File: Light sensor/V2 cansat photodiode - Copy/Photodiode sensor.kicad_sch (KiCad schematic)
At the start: 23 parts, among them IC1 MCP6004-I_SL, J1 Conn_01x02, J2 Conn_01x05, J3 Conn_01x04

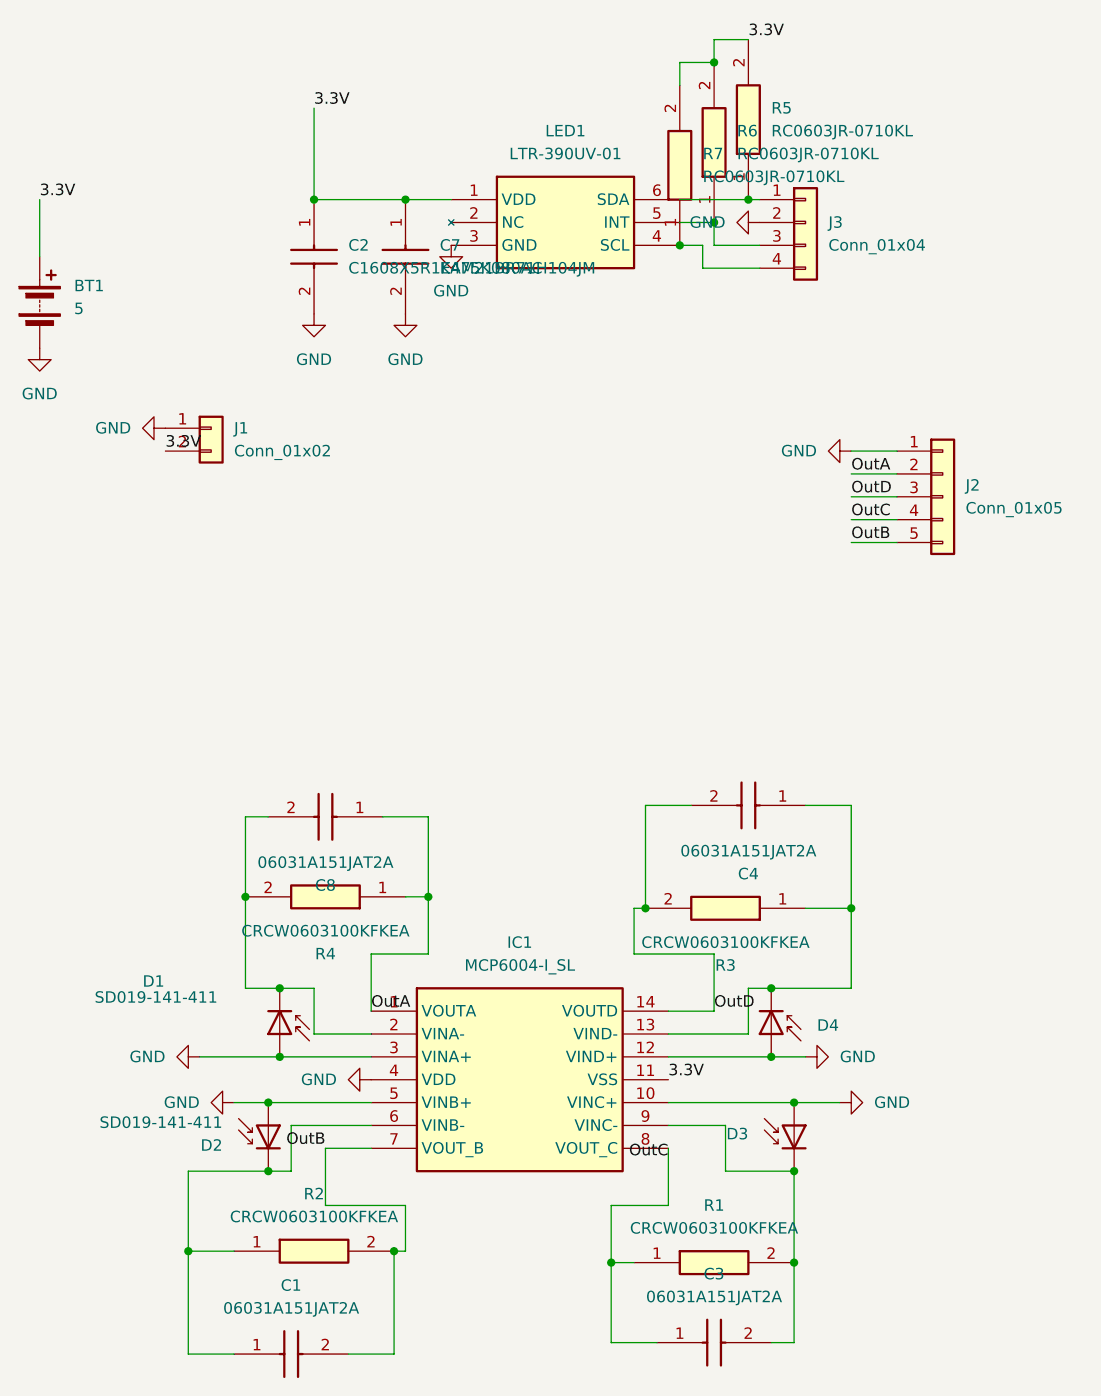
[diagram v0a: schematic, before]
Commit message: V4 photodiode sensor
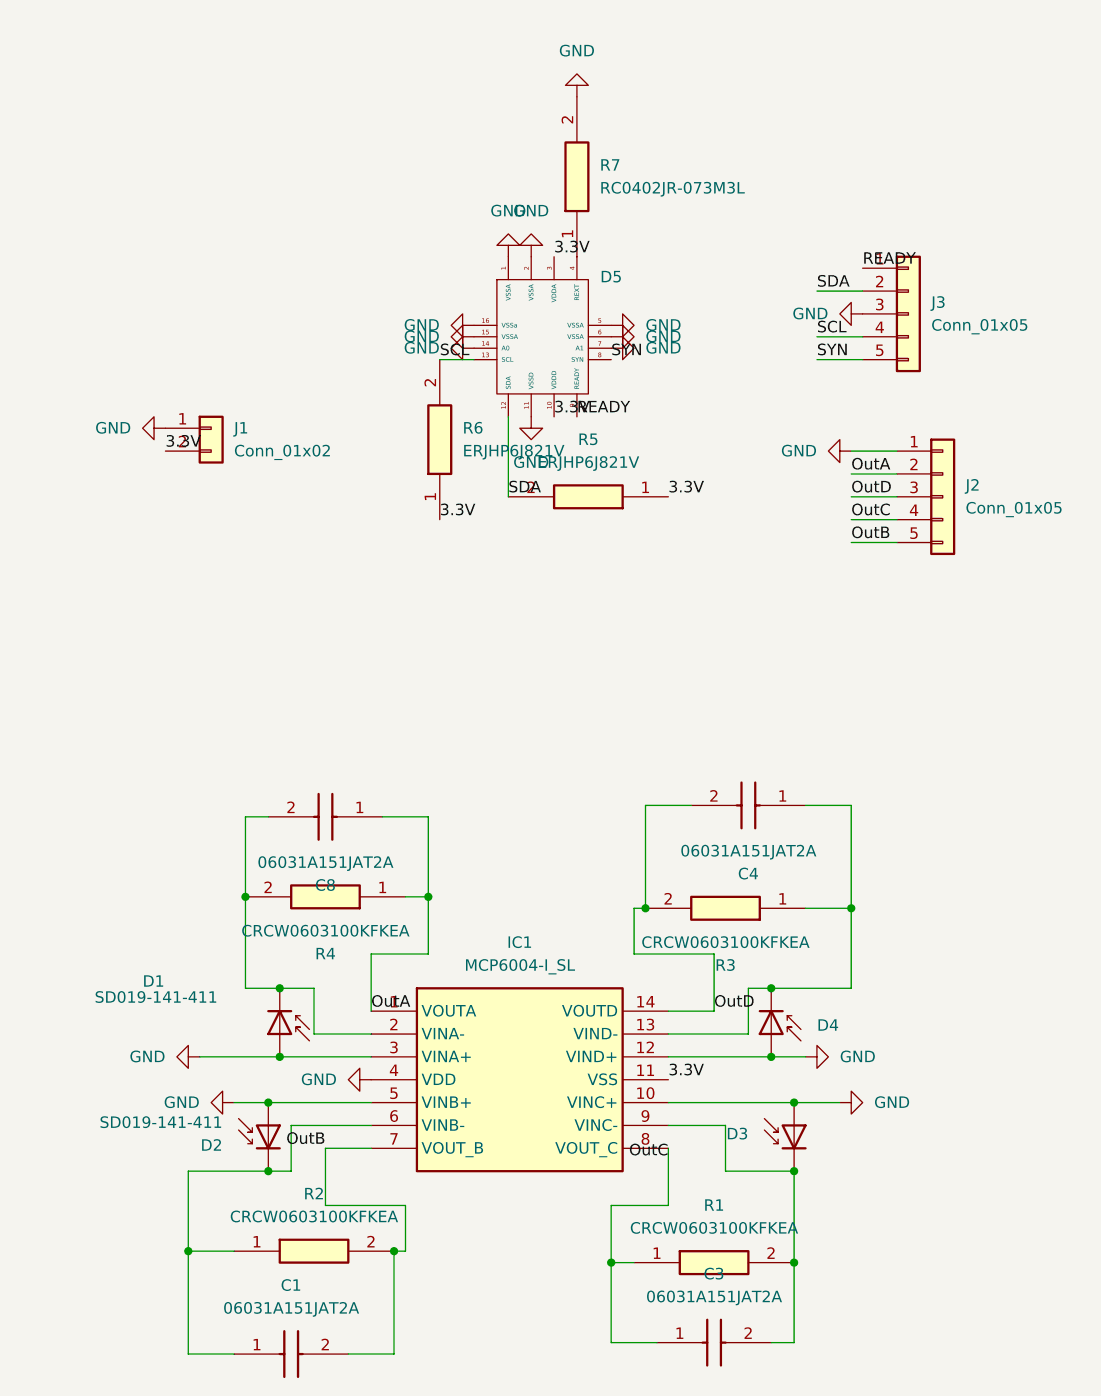
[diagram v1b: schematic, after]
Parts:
- removed BT1: 5, symbol Device:Battery
- removed C2: C1608X5R1E475K080AC, CUSTOM_LIBRARY:CAPC1608X80N, symbol CUSTOM_SYMBOL:C1608X5R1E475K080AC
- removed C7: KAM21BR71H104JM, CUSTOM_LIBRARY:CAPC2012X94N, symbol CUSTOM_SYMBOL:KAM21BR71H104JM
- removed J3: Conn_01x04, Connector_PinHeader_1.00mm:PinHeader_1x04_P1.00mm_Vertical, symbol Connector_Generic:Conn_01x04
- removed LED1: LTR-390UV-01, CUSTOM_LIBRARY:LTR390UV01, symbol CUSTOM_SYMBOL:LTR-390UV-01
- removed R5, R6, R7: RC0603JR-0710KL, RESC1608X55N, symbol CUSTOM_SYMBOL:RC0603JR-0710KL
- added D5: ~, CUSTOM_LIBRARY:AS7331-AQFM, symbol CUSTOM_SYMBOL:AS7331-AQFM
- added J3: Conn_01x05, Connector_PinHeader_1.00mm:PinHeader_1x05_P1.00mm_Vertical, symbol Connector_Generic:Conn_01x05
- added R5, R6: ERJHP6J821V, ERJHP6D1000V, symbol CUSTOM_SYMBOL:ERJHP6J821V
- added R7: RC0402JR-073M3L, ERJHP6D1000V, symbol CUSTOM_SYMBOL:RC0402JR-073M3L
- J1: footprint CUSTOM_LIBRARY:SHDR4W64P0X254_1X4_1020X580X1175P -> Connector_PinHeader_1.00mm:PinHeader_1x02_P1.00mm_Vertical
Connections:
- net 3.3V: now also D5.10 (VDDD), D5.3 (VDDA), R5.1, R6.1
- net GND: now also D5.1 (VSSA), D5.11 (VSSD), D5.14 (A0), D5.15 (VSSA), D5.16 (VSSa), D5.2 (VSSA), D5.5 (VSSA), D5.6 (VSSA), D5.7 (A1), J3.3 (Pin_3), R7.2
- new net: D5.4 (REXT), R7.1
- new net READY: D5.9 (READY), J3.1 (Pin_1)
- new net SCL: D5.13 (SCL), J3.4 (Pin_4), R6.2
- new net SDA: D5.12 (SDA), J3.2 (Pin_2), R5.2
- new net SYN: D5.8 (SYN), J3.5 (Pin_5)
